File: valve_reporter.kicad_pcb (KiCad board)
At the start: 2 copper layers, 96.5 x 71.1 mm, 58 parts, among them J1 Screw_Terminal_01x05, J2 Screw_Terminal_01x14, K1 G5LE-1, Q1 2N3904, U1 NodeMCU_1.0_(ESP-12E), U2 MC7805CTG

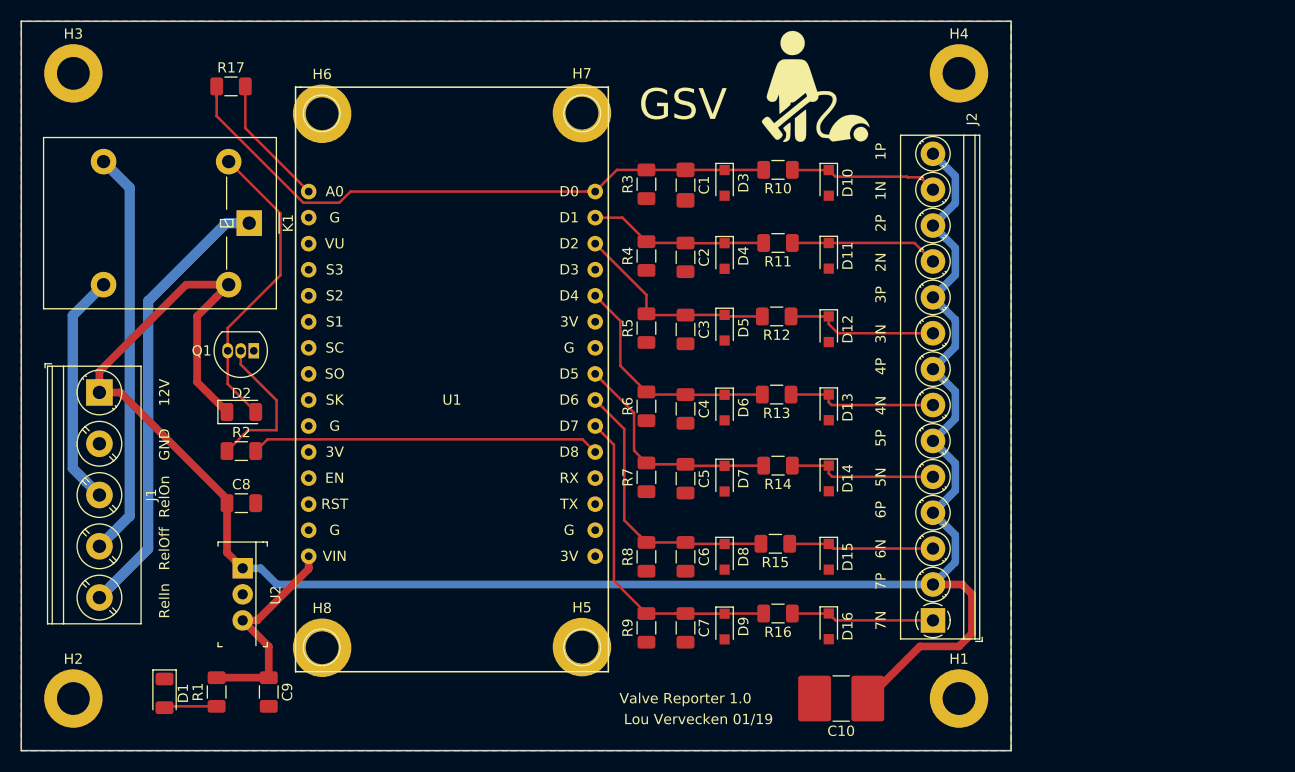
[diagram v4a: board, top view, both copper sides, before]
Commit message: Move to handsolder pads to make live easier
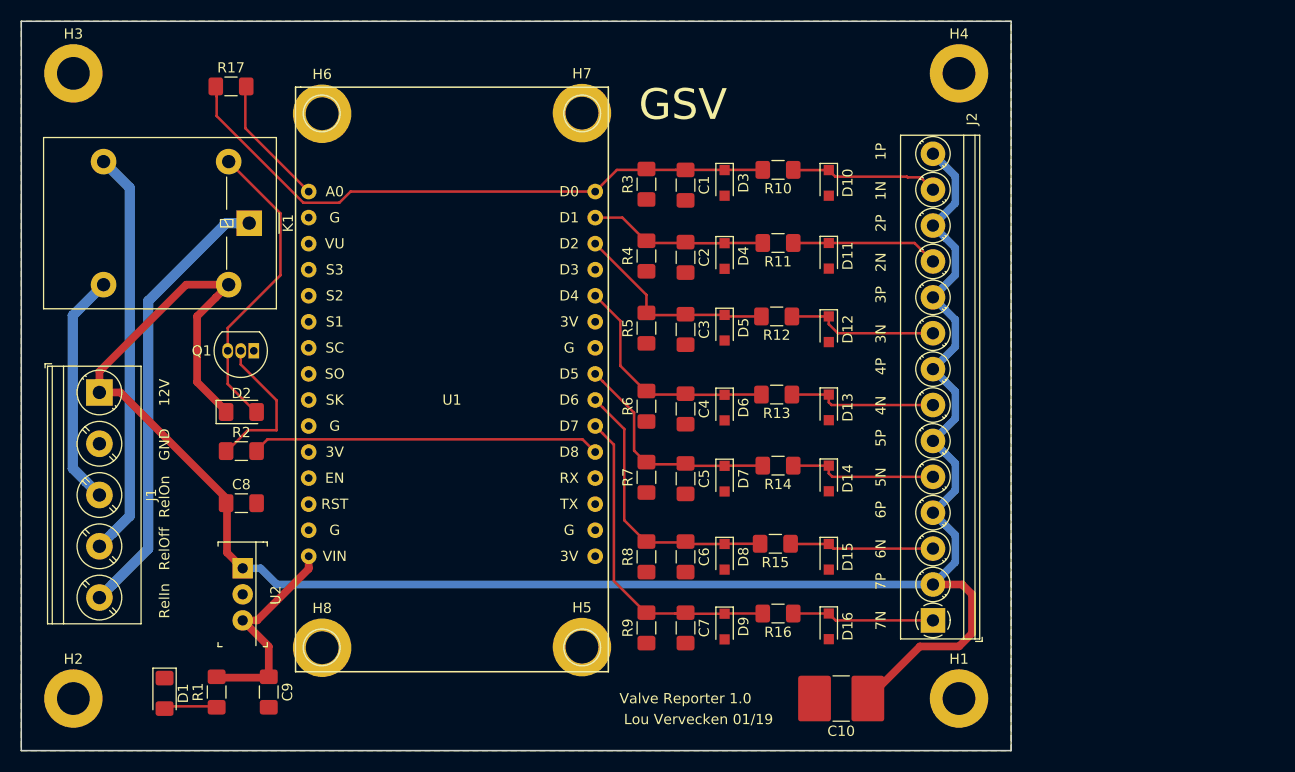
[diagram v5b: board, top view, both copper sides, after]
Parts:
- removed G***: LOGO, artwork:m_vac
- C2, C3, C4, C5, C6, C7, C8, C9: footprint Capacitor_SMD:C_1206_3216Metric -> Capacitor_SMD:C_1206_3216Metric_Pad1.42x1.75mm_HandSolder
- D1: footprint LED_SMD:LED_1206_3216Metric -> LED_SMD:LED_1206_3216Metric_Pad1.42x1.75mm_HandSolder
- D2: footprint Diode_SMD:D_1206_3216Metric -> Diode_SMD:D_1206_3216Metric_Pad1.42x1.75mm_HandSolder
- R1, R10, R11, R12, R13, R14, R15, R16, R17, R2, R3, R4, R5, R6, R7, R8, R9: footprint Resistor_SMD:R_1206_3216Metric -> Resistor_SMD:R_1206_3216Metric_Pad1.42x1.75mm_HandSolder

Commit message: Add artwork again
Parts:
- added G***: LOGO, artwork:m_vac, F.Cu at (157.5, 74.9)

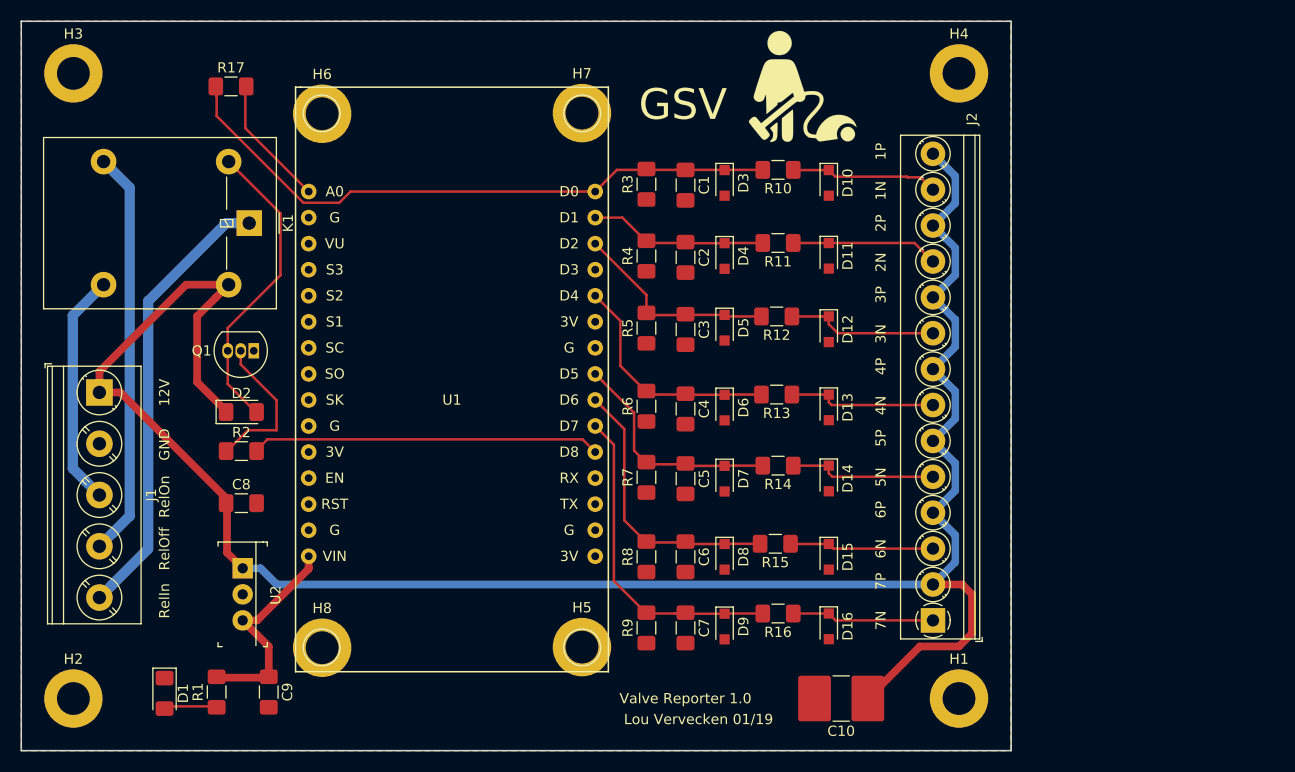
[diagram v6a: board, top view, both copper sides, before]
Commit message: Test points, 12V plane, fancy BOM
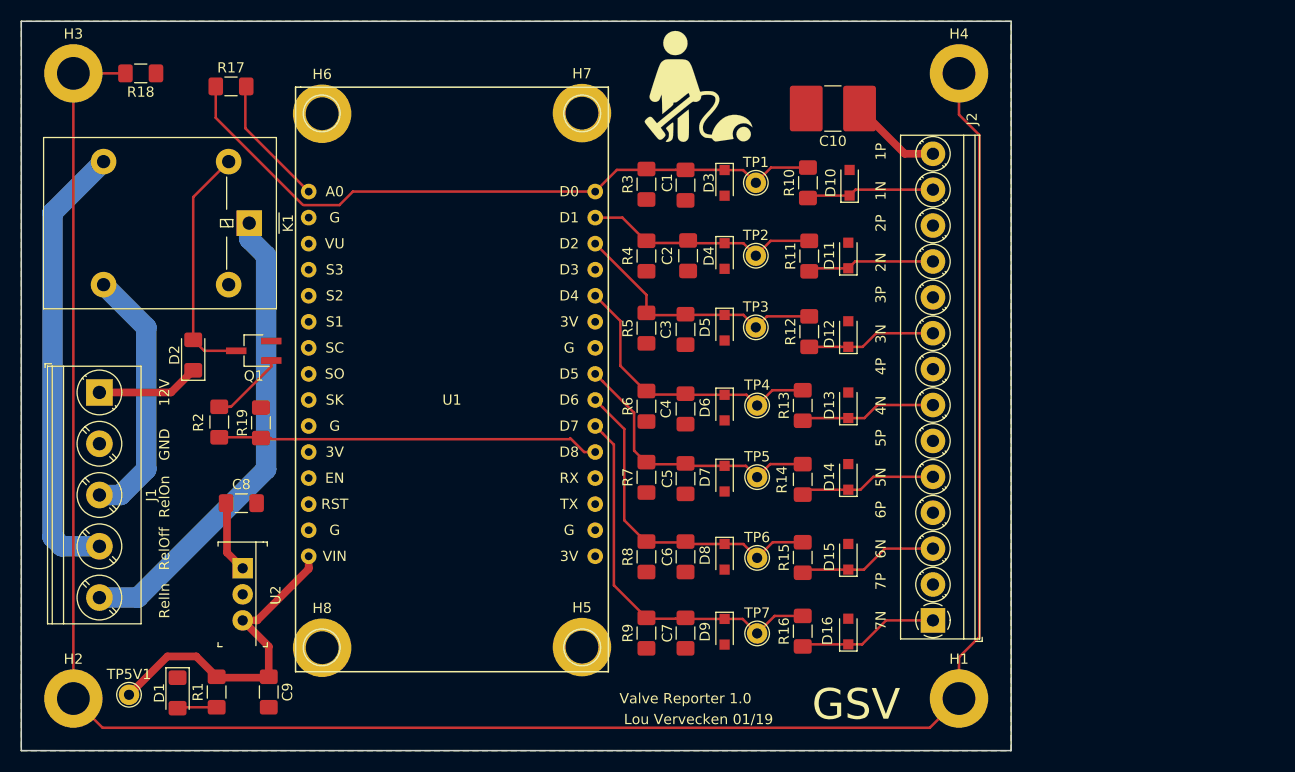
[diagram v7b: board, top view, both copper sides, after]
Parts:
- added R18: 1M, Resistor_SMD:R_1206_3216Metric_Pad1.42x1.75mm_HandSolder, F.Cu at (92.9, 73.7)
- added R19: 10k, Resistor_SMD:R_1206_3216Metric_Pad1.42x1.75mm_HandSolder, F.Cu at (104.6, 107.7)
- added TP1: TestPoint_Probe, TestPoint:TestPoint_THTPad_D2.0mm_Drill1.0mm, F.Cu at (152.9, 84.3)
- added TP2: TestPoint_Probe, TestPoint:TestPoint_THTPad_D2.0mm_Drill1.0mm, F.Cu at (152.9, 91.4)
- added TP3: TestPoint_Probe, TestPoint:TestPoint_THTPad_D2.0mm_Drill1.0mm, F.Cu at (152.9, 98.4)
- added TP4: TestPoint_Probe, TestPoint:TestPoint_THTPad_D2.0mm_Drill1.0mm, F.Cu at (153.0, 106.0)
- added TP5: TestPoint_Probe, TestPoint:TestPoint_THTPad_D2.0mm_Drill1.0mm, F.Cu at (153.0, 113.0)
- added TP5V1: TestPoint_Probe, TestPoint:TestPoint_THTPad_D2.0mm_Drill1.0mm, F.Cu at (91.8, 134.3)
- added TP6: TestPoint_Probe, TestPoint:TestPoint_THTPad_D2.0mm_Drill1.0mm, F.Cu at (153.0, 120.9)
- added TP7: TestPoint_Probe, TestPoint:TestPoint_THTPad_D2.0mm_Drill1.0mm, F.Cu at (153.0, 128.3)
- C10: value 50uF -> 100uF
- Q1: value 2N3904 -> FDV303N; footprint Package_TO_SOT_THT:TO-92_Inline -> Package_TO_SOT_SMD:TSOT-23_HandSoldering
- R2: value 2k -> 500
- moved C10 57.5 mm to (160.4, 77.1)
- moved G*** 10.2 mm to (147.3, 74.9)
- moved D2 7.27 mm to (98.0, 101.1), turned to 90 degrees
- moved R2 3.56 mm to (100.6, 107.7), turned to 270 degrees
- moved R12 3.50 mm to (158.1, 98.8), turned to 90 degrees
- moved R11 3.30 mm to (158.1, 91.5), turned to 90 degrees
- moved R10 3.18 mm to (158.0, 84.3), turned to 90 degrees
- moved R15 2.99 mm to (157.5, 120.9), turned to 90 degrees
- moved R16 2.96 mm to (157.5, 128.1), turned to 90 degrees
- moved R14 2.76 mm to (157.5, 113.2), turned to 90 degrees
- moved R13 2.75 mm to (157.5, 106.0), turned to 90 degrees
- moved D10 2.03 mm to (162.1, 84.3), turned to 90 degrees
- moved D16 1.97 mm to (161.9, 128.1), turned to 90 degrees
- moved D12 1.96 mm to (161.9, 99.1), turned to 90 degrees
- moved D13 1.92 mm to (161.9, 106.0), turned to 90 degrees
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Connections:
- H1 pad 1: GND -> Net-(H1-Pad1)
- H2 pad 1: GND -> Net-(H1-Pad1)
- H3 pad 1: GND -> Net-(H1-Pad1)
- H4 pad 1: GND -> Net-(H1-Pad1)
- Q1 pad 1: GND -> Net-(Q1-Pad1)
- Q1 pad 2: Net-(Q1-Pad2) -> GND
- R2 pad 1: Net-(Q1-Pad2) -> Net-(Q1-Pad1)
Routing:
- net Net-(H1-Pad1): track 0.00 -> 217.4 mm
- net +12V: track 198.8 -> 26.0 mm
- net Net-(Q1-Pad2): track 14.9 -> 0.00 mm
- net +5V: track 21.5 -> 32.4 mm
- net Net-(Q1-Pad1): track 0.00 -> 7.28 mm
- net Net-(D2-Pad2): track 29.8 -> 23.4 mm
- net Net-(C1-Pad1): track 61.6 -> 67.3 mm
- net Net-(C2-Pad1): track 17.9 -> 23.5 mm
- net Net-(C7-Pad1): track 32.3 -> 37.8 mm
- net Net-(C3-Pad1): track 20.5 -> 26.0 mm
- net Net-(C6-Pad1): track 28.9 -> 34.1 mm
- net Net-(C4-Pad1): track 23.3 -> 28.3 mm
- net Net-(C5-Pad1): track 23.0 -> 27.8 mm
- net /RelOff: track 39.8 -> 43.6 mm
- net Net-(R19-Pad1): track 34.1 -> 37.3 mm
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- added copper zone on B.Cu, net +12V
- removed copper zone on B.Cu, net GND
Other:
- net class Relay: clearance 0.8 -> 1; trace_width 1 -> 2
